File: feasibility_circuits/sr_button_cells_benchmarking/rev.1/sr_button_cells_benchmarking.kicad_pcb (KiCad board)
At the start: 2 copper layers, 88.5 x 47 mm, 50 parts, among them J1 Current Measurement, J10 Jumper, J11 EN_MED_CURR, J12 Jumper, J13 BATT+, J2 EN_POT, J3 GND, J4 GND, J5 Jumper, J6 VIN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

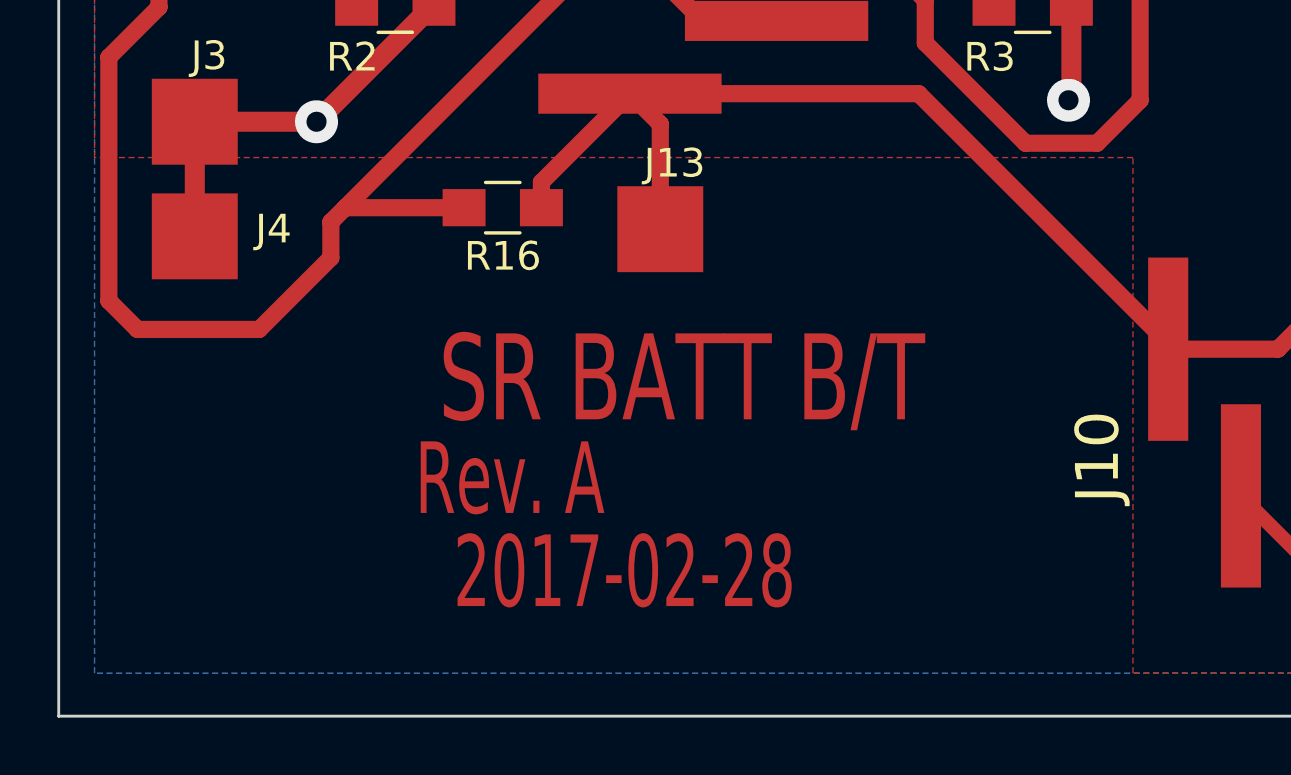
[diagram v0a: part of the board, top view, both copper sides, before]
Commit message: Review and organisation
Review of Auxiliary PIC and IR barrier setup board. Organisation of
resources.
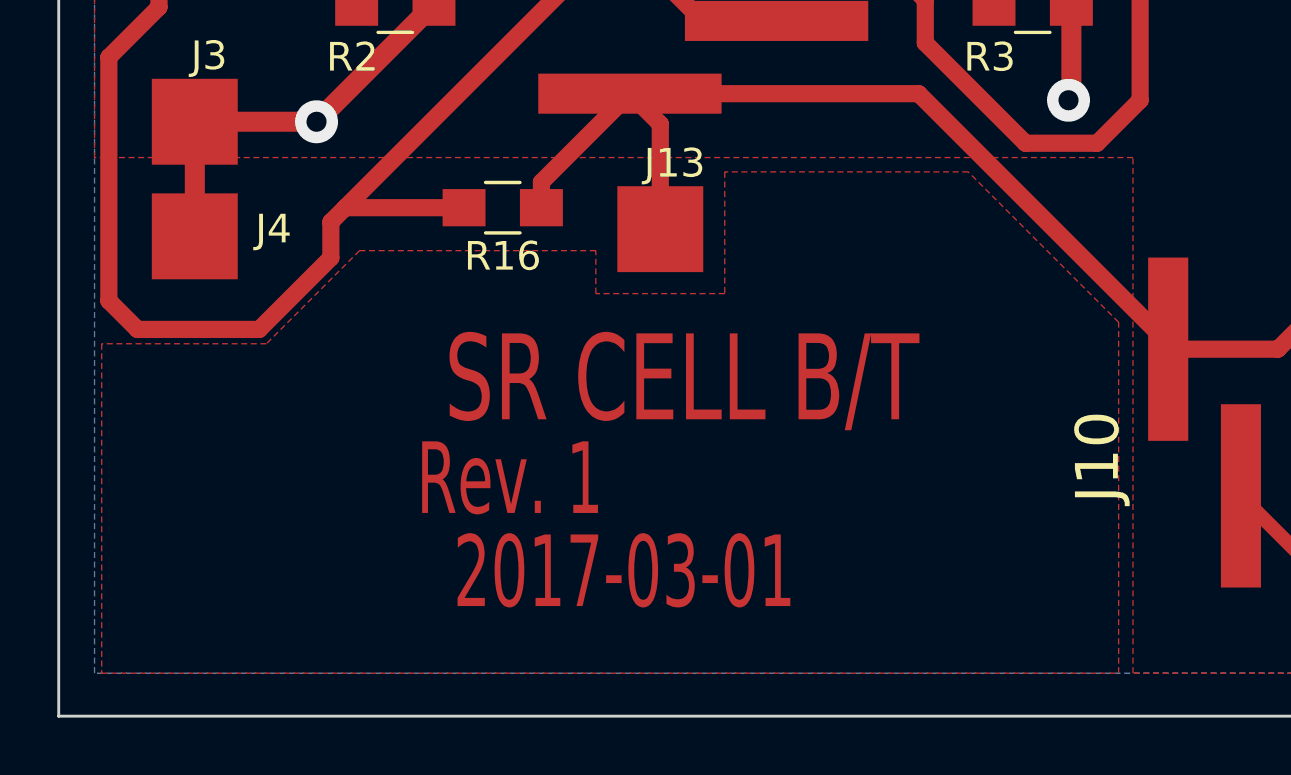
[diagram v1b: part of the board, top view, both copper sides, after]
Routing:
- added copper zone on F.Cu, net (none)
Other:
- board text added: "2017-03-01"
- board text added: "Rev. 1"
- board text added: "SR CELL B/T"
- board text removed: "2017-02-28"
- board text removed: "Rev. A"
- board text removed: "SR BATT B/T"
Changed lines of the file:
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@@
   (page A4)
   (title_block
-    (title "Silver-Oxide Batteries Benchmarking/Testing")
-    (rev A)
+    (title "Silver-Oxide Button Cells Benchmarking/Testing")
+    (date 2017-03-01)
+    (rev 1)
     (company "HotSwap Norden AB")
-    (comment 1 "Short title: SR BATT B/T")
-    (comment 2 "Designed by: Khurram")
-    (comment 3 "Reviewed by: Rickard")
+    (comment 1 "Short title: SR CELL B/T")
+    (comment 2 "Designed by: khyo")
+    (comment 3 "Reviewed by: rigu")
   )
   (layers
@@
   )
   (setup
-    (last_trace_width 0.6)
+    (last_trace_width 0.4)
     (user_trace_width 0.2)
     (user_trace_width 0.3)
@@
     )
   )
+  (gr_text 2017-03-01 (at 52.75 69) (layer F.Cu)
+    (effects (font (size 2.5 1.5) (thickness 0.3)))
+  )
   (gr_line (start 33 74) (end 33 27) (angle 90) (layer Edge.Cuts) (width 0.1))
   (gr_line (start 121.5 74) (end 33 74) (angle 90) (layer Edge.Cuts) (width 0.1))
   (gr_line (start 121.5 27) (end 121.5 74) (angle 90) (layer Edge.Cuts) (width 0.1))
   (gr_line (start 33 27) (end 121.5 27) (angle 90) (layer Edge.Cuts) (width 0.1))
-  (gr_text 2017-02-28 (at 52.75 69) (layer F.Cu)
+  (gr_text "Rev. 1" (at 48.75 65.75) (layer F.Cu)
     (effects (font (size 2.5 1.5) (thickness 0.3)))
   )
-  (gr_text "Rev. A" (at 48.75 65.75) (layer F.Cu)
-    (effects (font (size 2.5 1.5) (thickness 0.3)))
-  )
-  (gr_text "SR BATT B/T" (at 54.75 62.25) (layer F.Cu)
+  (gr_text "SR CELL B/T" (at 54.75 62.25) (layer F.Cu)
     (effects (font (size 3 2) (thickness 0.4)))
   )
@@
     (effects (font (size 3 3) (thickness 0.4)))
   )
-  (segment (start 47.15 56.25) (end 43 56.25) (width 0.6) (layer F.Cu) (net 1) (status 400000))
+  (segment (start 47.15 56.25) (end 43 56.25) (width 0.6) (layer F.Cu) (net 1))
   (segment (start 58.06 49.73) (end 55.48 49.73) (width 0.6) (layer F.Cu) (net 1))
   (segment (start 55.48 49.73) (end 52.5 46.75) (width 0.6) (layer F.Cu) (net 1))
@@
   (segment (start 109.15 66.75) (end 109.15 66.45) (width 0.4) (layer F.Cu) (net 18))
   (segment (start 109.15 66.45) (end 111.85 63.75) (width 0.4) (layer F.Cu) (net 18))
-  (segment (start 49.85 56.25) (end 49.85 55.36) (width 0.6) (layer F.Cu) (net 19) (status 400000))
-  (segment (start 49.85 55.36) (end 52.94 52.27) (width 0.6) (layer F.Cu) (net 19) (status 800000))
-  (segment (start 54 57) (end 54 53.33) (width 0.6) (layer F.Cu) (net 19) (status 400000))
-  (segment (start 54 53.33) (end 52.94 52.27) (width 0.6) (layer F.Cu) (net 19) (status 800000))
+  (segment (start 49.85 56.25) (end 49.85 55.36) (width 0.6) (layer F.Cu) (net 19))
+  (segment (start 49.85 55.36) (end 52.94 52.27) (width 0.6) (layer F.Cu) (net 19))
+  (segment (start 54 57) (end 54 53.33) (width 0.6) (layer F.Cu) (net 19))
+  (segment (start 54 53.33) (end 52.94 52.27) (width 0.6) (layer F.Cu) (net 19))
   (segment (start 101.48 61.19) (end 103.31 61.19) (width 0.6) (layer F.Cu) (net 19))
   (segment (start 107.75 49.96) (end 109.94 47.77) (width 0.6) (layer F.Cu) (net 19))
@@
       )
     )
+  )
+  (zone (net 0) (net_name "") (layer F.Cu) (hatch edge 0.508)
+    (connect_pads (clearance 0.5))
+    (min_thickness 1.5)
+    (fill yes (arc_segments 16) (thermal_gap 0.4) (thermal_bridge_width 1.6) (smoothing chamfer) (radius 0.3))
+    (polygon
+      (pts
+        (xy 70 72.5) (xy 70 60.25) (xy 64.75 55) (xy 56.25 55) (xy 56.25 59.25)
+        (xy 51.75 59.25) (xy 51.75 57.75) (xy 43.5 57.75) (xy 40.25 61) (xy 34.5 61)
+        (xy 34.5 72.5) (xy 36.5 72.5)
+      )
+    )
